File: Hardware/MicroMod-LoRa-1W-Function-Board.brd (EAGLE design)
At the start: 67.5 x 38 mm, 48 parts, among them J11 MICROMOD_STANDARD, Q3 20V/4.2A/52mΩ/1.4W, Q4 600mA/40V, Q5 20V/4.2A/52mΩ/1.4W, Q6 600mA/40V, U1 EEPROM, U4 E19-915M30S

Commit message: Adding panel files
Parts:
- added LOGO2: SPECIAL_INSTRUCTIONS-ORDERING, SparkFun-Aesthetics:ORDERING_INSTRUCTIONS
- added U$8: (no value), output:FUNCTION#0
- added U$9: (no value), output:#PWR#0
- C8: value 68uF -> 47uF
- J11: device SparkFun-MicroMod-Test:M.2-CARD-E-22_FUNCTION_STANDARD -> SparkFun-MicroMod-Function:M.2-CARD-E-22_FUNCTION_STANDARD
- U$4: device output:#PWR#0 -> output:FUNCTION#0
- moved E1 83.0 mm to (26.1, 65.0), turned to 0 degrees
- moved FD2 79.6 mm to (1.05, 64.0), turned to 90 degrees
- moved FD4 79.6 mm to (1.05, 64.0), turned to 270 degrees
- moved H1 77.5 mm to (34.3, 57.1), turned to 90 degrees
- moved U$2 73.2 mm to (4.19, 58.9), turned to 90 degrees
- moved LOGO3 70.2 mm to (34.3, 52.1), turned to 270 degrees
- moved U$6 67.8 mm to (7.49, 59.8), turned to 90 degrees
- moved U$3 64.5 mm to (9.53, 59.7), turned to 90 degrees
- moved U$5 60.5 mm to (4.19, 54.1), turned to 90 degrees
- moved U$4 52.0 mm to (20.3, 35.6), turned to 270 degrees
- moved R18 51.6 mm to (35.1, 35.6), turned to 180 degrees
- moved R19 49.0 mm to (35.1, 33.0), turned to 180 degrees
- moved R17 46.5 mm to (35.2, 30.5), turned to 0 degrees
- moved C2 41.1 mm to (35.1, 24.3), turned to 270 degrees
- moved U$29 40.4 mm to (22.9, 34.8), turned to 270 degrees
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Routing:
- net LORA_!RST!: track 33.8 -> 29.7 mm
- net LORA_D0: track 39.9 -> 36.1 mm
- net LORA_D2: track 46.9 -> 43.5 mm
- net LORA_D1: track 42.4 -> 39.2 mm
- net LORA_RXEN: track 56.6 -> 54.1 mm
- net SPI_CIPO: track 34.6 -> 32.1 mm
- net SPI_SCK: track 30.8 -> 28.3 mm
- net SPI_COPI: track 37.1 -> 34.6 mm
- net LORA_TXEN: track 53.4 -> 50.9 mm
- net LORA_!CS!: track 52.7 -> 50.3 mm
- net PWR_EN: track 17.8 -> 16.6 mm
- net N$6: track 4.20 -> 3.29 mm
- net GND: vias 40 -> 46
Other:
- board size 67.5 x 38 mm -> 38 x 65 mm
- board text added: "2-Layer"
- board text added: "Beveled Edge"
- board text added: "Board Thickness is 0.8mm"
- board text added: "ENIG Finish"

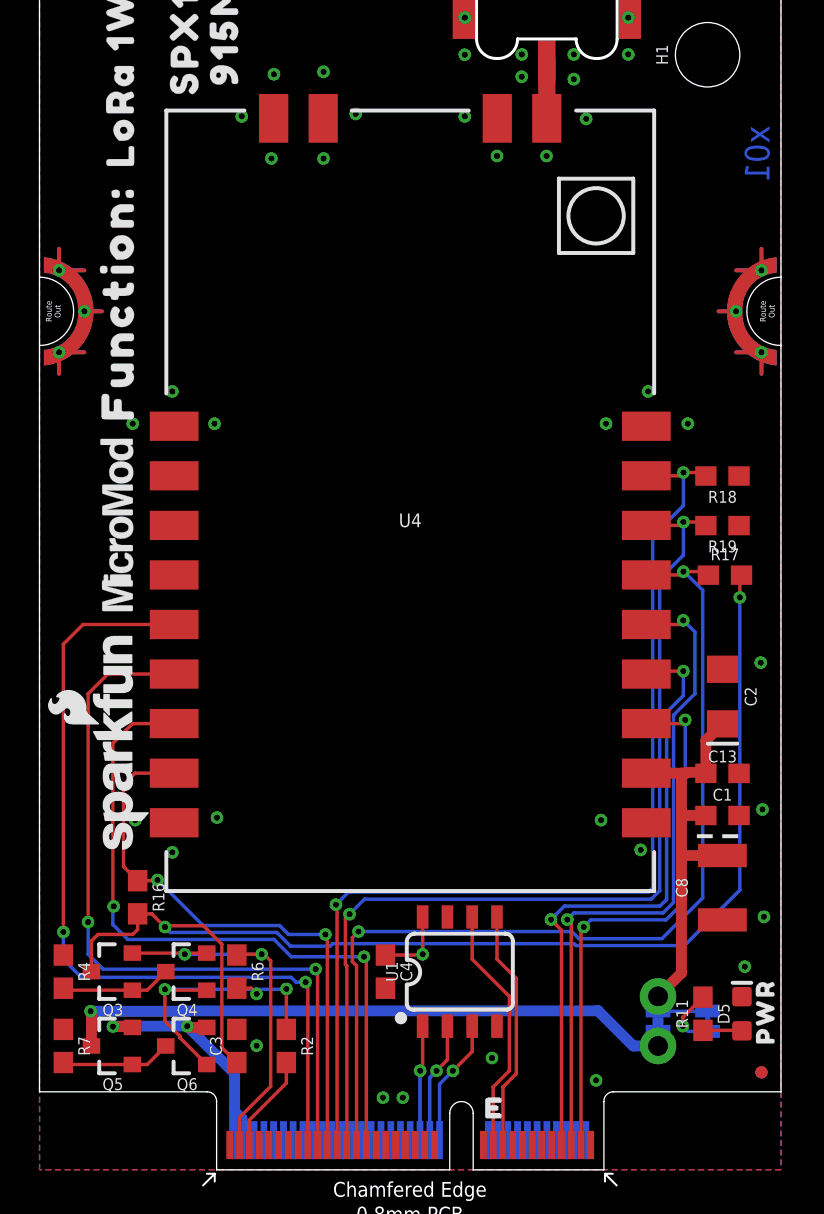
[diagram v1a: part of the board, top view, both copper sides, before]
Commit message: Fix power control circuit. Add example sketch. Add x02 production panels.
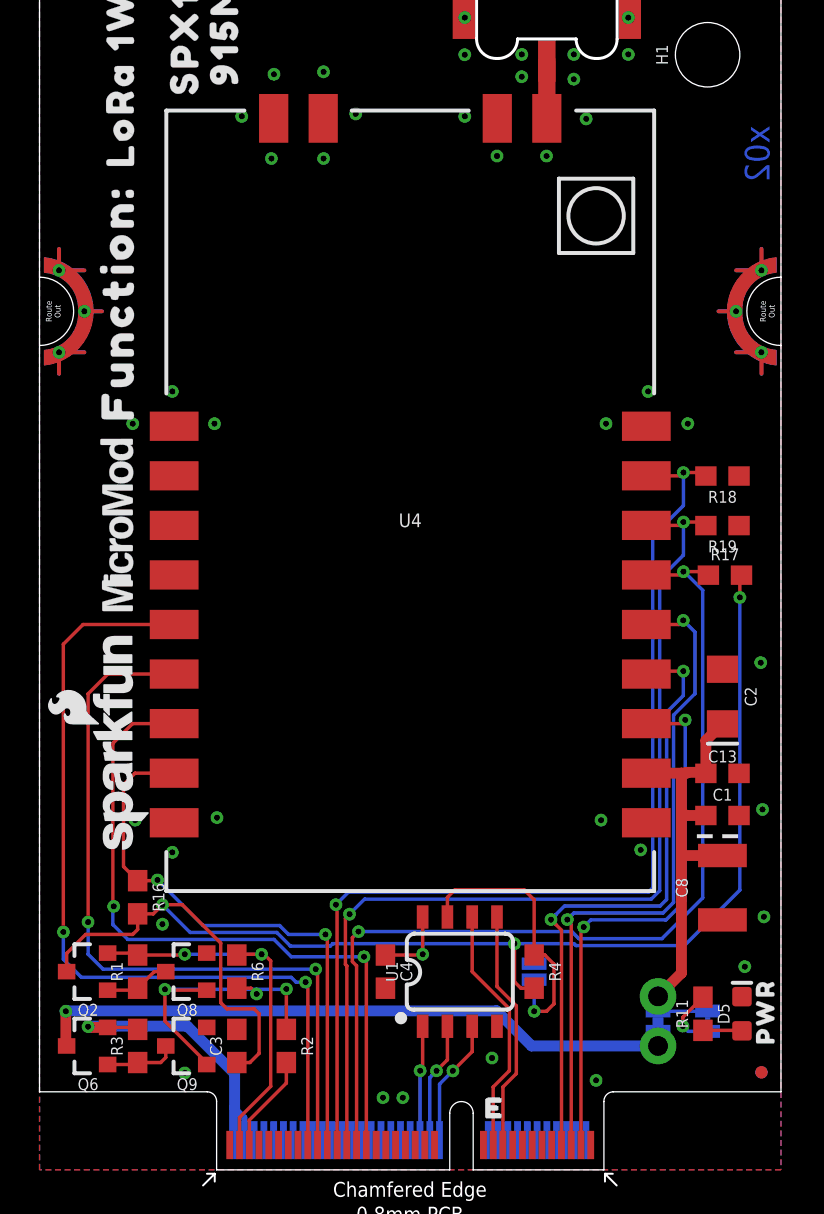
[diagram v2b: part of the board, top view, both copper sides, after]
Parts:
- removed Q3, Q5: 20V/4.2A/52mΩ/1.4W, SparkFun-DiscreteSemi:SOT23-3
- removed R7: 100k, SparkFun-Resistors:0603
- added JP1: (no value), SparkFun-Jumpers:SMT-JUMPER_2_NO_SILK
- added Q2: 20V/4.2A/52mΩ/1.4W, SparkFun-DiscreteSemi:SOT23-3
- added Q9: 5.8A/30V/35mΩ, SparkFun-DiscreteSemi:SOT23-3
- added R1, R3: 10k, SparkFun-Resistors:0603
- added U$10: (no value), output:#WP#0
- Q6: value 600mA/40V -> 20V/4.2A/52mΩ/1.4W
- Q8: value 600mA/40V -> 5.8A/30V/35mΩ
- R4: value 100k -> 10k
- moved R4 24.1 mm to (25.4, 10.2)
- moved Q6 5.08 mm to (2.54, 6.35)
- renumbered Q4 to Q8
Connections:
- removed net N$11: Q5.1, Q6.3, R7.2
- removed net N$9: Q3.1, Q8.3, R4.2
- new net N$2: Q2.1, Q8.3, R1.1
- new net N$3: Q6.1, Q9.3, R3.1
- new net N$7: JP1.2, R4.1, U1.7
- net 3.3V: now also Q2.3, R4.2; no longer Q3.3
- net 3.3V_IN: now also Q2.2, R1.2; no longer Q3.2, Q8.2
- net GND: now also JP1.1, Q8.2, Q9.2; no longer R4.1, R7.1, U1.7
- net PWR_EN: now also Q9.1; no longer Q6.1
- net VCC: now also Q6.3; no longer Q5.3
- net VCC_IN: now also R3.2; no longer Q5.2
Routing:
- net N$7: track 0.00 -> 14.7 mm, vias 0 -> 1
- net 3.3V: track 68.1 -> 75.2 mm, vias 3 -> 4
- net N$9: track 5.68 -> 0.00 mm
- net N$11: track 5.68 -> 0.00 mm
- net N$3: track 0.00 -> 3.72 mm
- net N$2: track 0.00 -> 3.37 mm
- net VCC_IN: track 14.6 -> 16.4 mm, vias 2 -> 1
- net VCC: track 32.4 -> 33.7 mm
- net GND: vias 46 -> 47
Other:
- board text added: "x02"
- board text removed: "x01"

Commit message: Add WP access to card edge.
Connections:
- removed net N$7: JP1.2, R4.1, U1.7
- new net EWP: J11.40, JP1.2, R4.1, U1.7
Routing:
- net EWP: track 0.00 -> 28.9 mm, vias 0 -> 3
- net N$7: track 14.7 -> 0.00 mm, vias 1 -> 0
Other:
- board text added: "x03"
- board text removed: "x02"

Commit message: Update version to v10.
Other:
- board text added: "v10"
- board text removed: "x03"
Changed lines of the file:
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@@
 <plain>
 <wire x1="28.975" y1="0" x2="22.275" y2="0" width="0.05" layer="20"/>
-<text x="36.83" y="52.07" size="1.27" layer="16" font="vector" ratio="20" rot="SMR270" align="center">x03</text>
+<text x="36.83" y="52.07" size="1.27" layer="16" font="vector" ratio="20" rot="SMR270" align="center">v10</text>
 <text x="34.29" y="-27.94" size="1.778" layer="51" font="vector" ratio="15">N. Seidle</text>
 <wire x1="21.075" y1="0" x2="9.125" y2="0" width="0.05" layer="20"/>

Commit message: Add SMA center pin. Increase panel gap to facilitate center pin. PCB is still v10.
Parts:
- JP1: value (none) -> JUMPER-SMT_2_NO_SILK
- MEAS: value (none) -> JUMPER-COMBO_2_NC_TRACE
- PWR_LED: value (none) -> JUMPER-SMT_2_NC_TRACE_SILK

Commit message: Updates the design to use the Micromod-function device in the official SFE Eagle Libs
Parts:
- J11: value MICROMOD_STANDARD -> MICROMOD_FUNCTION_STANDARD; device SparkFun-MicroMod-Function:M.2-CARD-E-22_FUNCTION_STANDARD -> SparkFun-MicroMod:M.2-CARD-E-22_FUNCTION_STANDARD
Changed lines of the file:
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@@
 <?xml version="1.0" encoding="utf-8"?>
 <!DOCTYPE eagle SYSTEM "eagle.dtd">
-<eagle version="9.6.2">
+<eagle version="9.5.2">
 <drawing>
 <settings>
-<setting alwaysvectorfont="yes"/>
+<setting alwaysvectorfont="no"/>
 <setting verticaltext="up"/>
 </settings>
@@
 <attribute name="PROD_ID" value="CONN-15101" x="26.05" y="64.96" size="1.778" layer="27" font="vector" ratio="15" display="off"/>
 </element>
-<element name="J11" library="SparkFun-MicroMod-Function" package="M.2-CARD-E-22_FUNCTION_STANDARD" value="MICROMOD_STANDARD" x="19.05" y="0" smashed="yes"/>
+<element name="J11" library="SparkFun-MicroMod" package="M.2-CARD-E-22_FUNCTION_STANDARD" value="MICROMOD_FUNCTION_STANDARD" x="19.05" y="0" smashed="yes"/>
 <element name="R2" library="SparkFun-Resistors" package="0603" value="470" x="12.7" y="6.35" smashed="yes" rot="R270">
 <attribute name="NAME" x="13.462" y="6.35" size="0.6096" layer="25" font="vector" ratio="20" rot="R270" align="bottom-center"/>
